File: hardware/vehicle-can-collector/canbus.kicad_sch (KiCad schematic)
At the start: 26 parts, among them Q701 2N7002, U701 MCP2557FD-xMF, U702 TH8056KDC-AAA-008-RE, U703 MCP2515-xSO, U704 MCP2557FD-xMF, U705 TCA9534

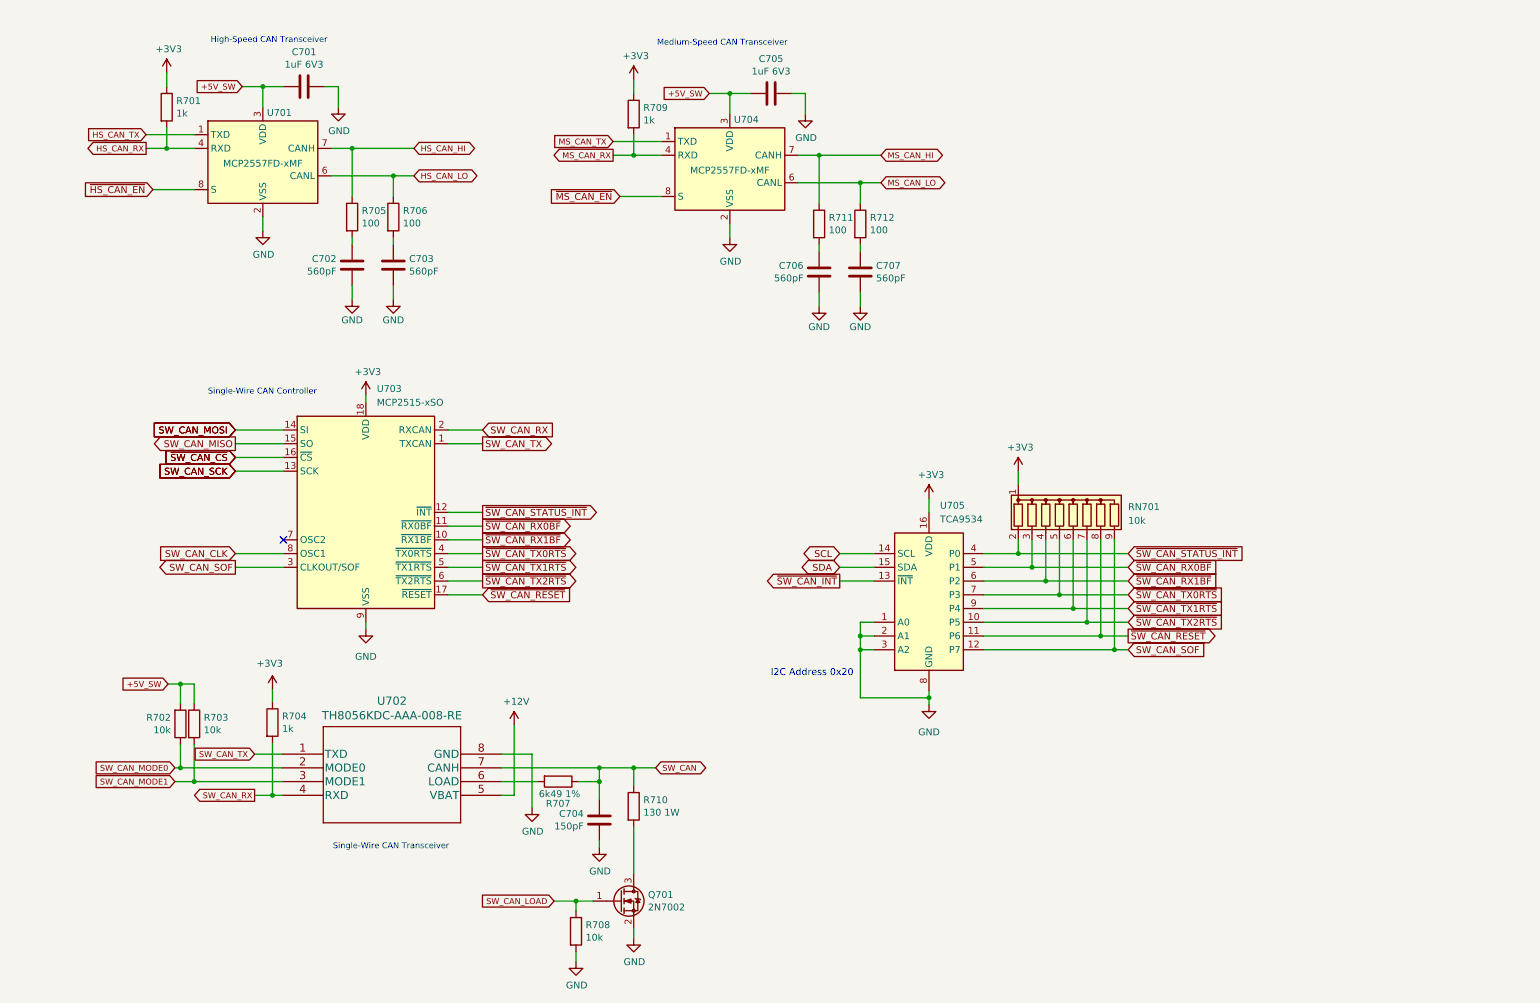
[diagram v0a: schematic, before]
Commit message: Added decoupling, more LEDs, update dts
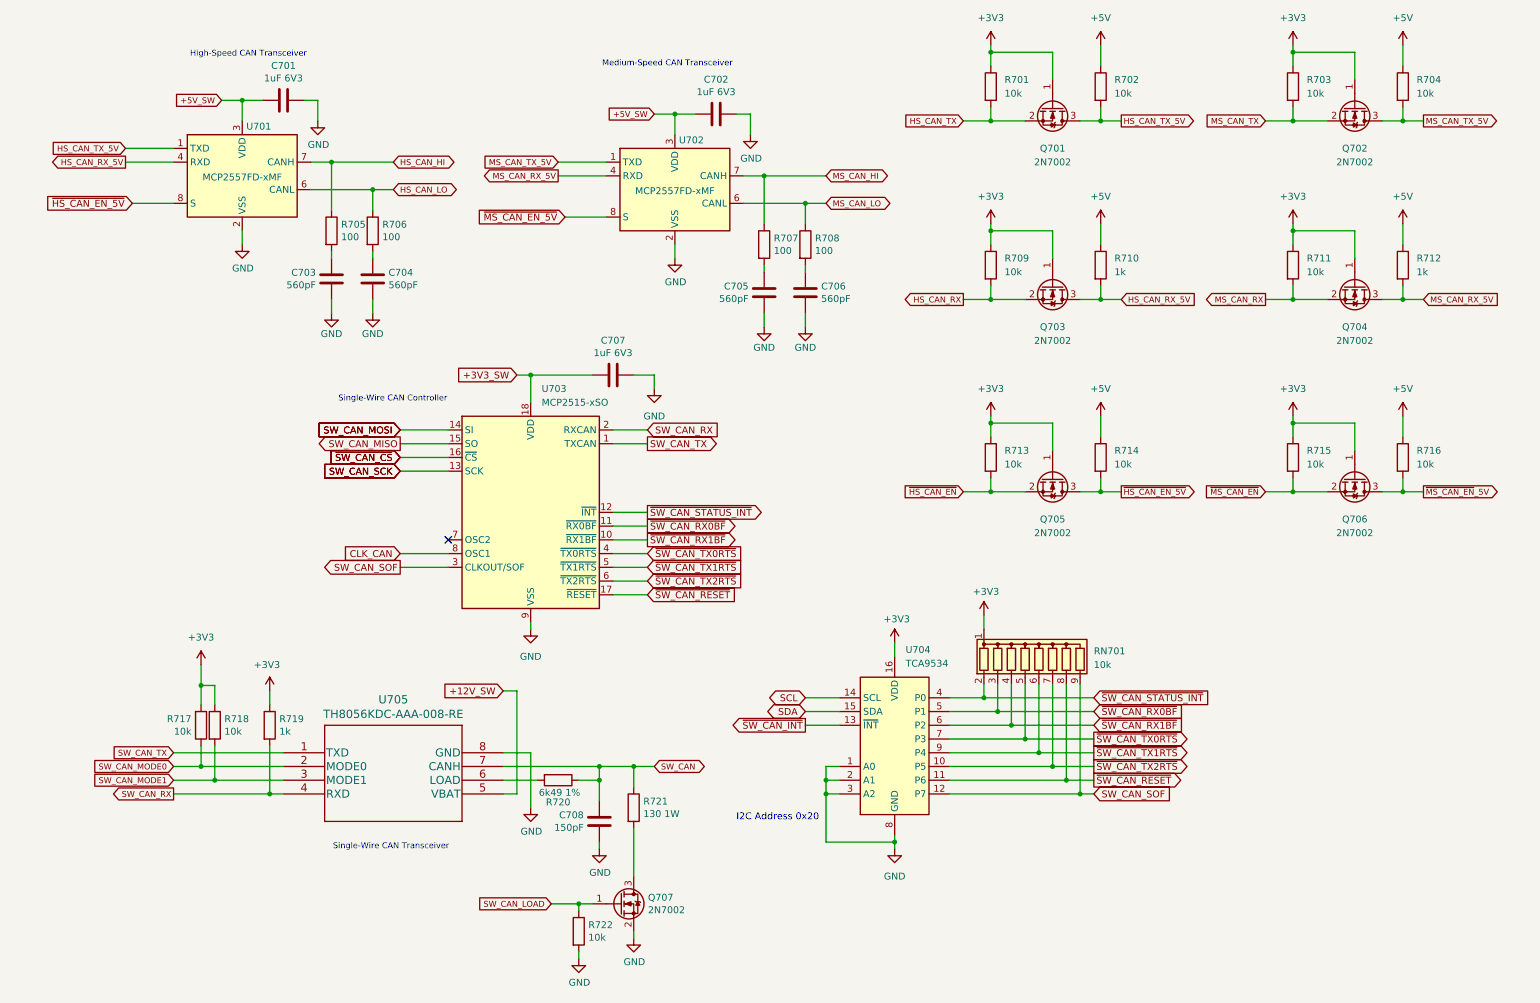
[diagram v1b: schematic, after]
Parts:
- added C707: 1uF 6V3, symbol Device:C
- added Q701, Q702, Q703, Q704, Q705, Q706: 2N7002, Package_TO_SOT_SMD:SOT-23, symbol Transistor_FET:2N7002
- added R702, R703, R704, R711, R713, R714, R715, R716: 10k, symbol Device:R
- added R710, R712: 1k, symbol Device:R
- R701, R709: value 1k -> 10k
- renumbered C705 to C702, C702 to C703, C703 to C704, C706 to C705, C707 to C706, C704 to C708, Q701 to Q707, R711 to R707, R712 to R708, R702 to R717, R703 to R718, R704 to R719, R707 to R720, R710 to R721, R708 to R722, U704 to U702, U705 to U704, U702 to U705
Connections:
- net +3V3: now also R717.2, R718.1, Q701.1 (G), Q702.1 (G), Q703.1 (G), Q704.1 (G), Q705.1 (G), Q706.1 (G), R703.1, R711.1, R713.1, R715.1; no longer U703.18 (VDD)
- net +5V_SW: no longer R717.2, R718.1
- net GND: now also C707.1
- net HS_CAN_RX: now also R709.2, Q703.2 (S); no longer R701.2, U701.4 (RXD)
- net HS_CAN_TX: now also R701.2, Q701.2 (S); no longer U701.1 (TXD)
- net MS_CAN_RX: now also Q704.2 (S), R711.2; no longer R709.2, U702.4 (RXD)
- net MS_CAN_TX: now also Q702.2 (S), R703.2; no longer U702.1 (TXD)
- net ~{HS_CAN_EN}: now also Q705.2 (S), R713.2; no longer U701.8 (S)
- net ~{MS_CAN_EN}: now also Q706.2 (S), R715.2; no longer U702.8 (S)
- net +12V renamed +12V_SW
- net SW_CAN_CLK renamed CLK_CAN
- new net +3V3_SW: C707.2, U703.18 (VDD)
- new net +5V: R702.1, R704.1, R710.1, R712.1, R714.1, R716.1
- new net HS_CAN_RX_5V: Q703.3 (D), R710.2, U701.4 (RXD)
- new net HS_CAN_TX_5V: Q701.3 (D), R702.2, U701.1 (TXD)
- new net MS_CAN_RX_5V: Q704.3 (D), R712.2, U702.4 (RXD)
- new net MS_CAN_TX_5V: Q702.3 (D), R704.2, U702.1 (TXD)
- new net ~{HS_CAN_EN_5V}: Q705.3 (D), R714.2, U701.8 (S)
- new net ~{MS_CAN_EN_5V}: U702.8 (S)
- new net ~{MS_CAN_EN}_5V: Q706.3 (D), R716.2
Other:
- company: (none) -> Gavin Hurlbut
- title: (none) -> Vehicle CAN Collector
- moved on the sheet: C701, C702, C703, C704, C705, C706, Q707, R705, R706, R707, R708, R717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

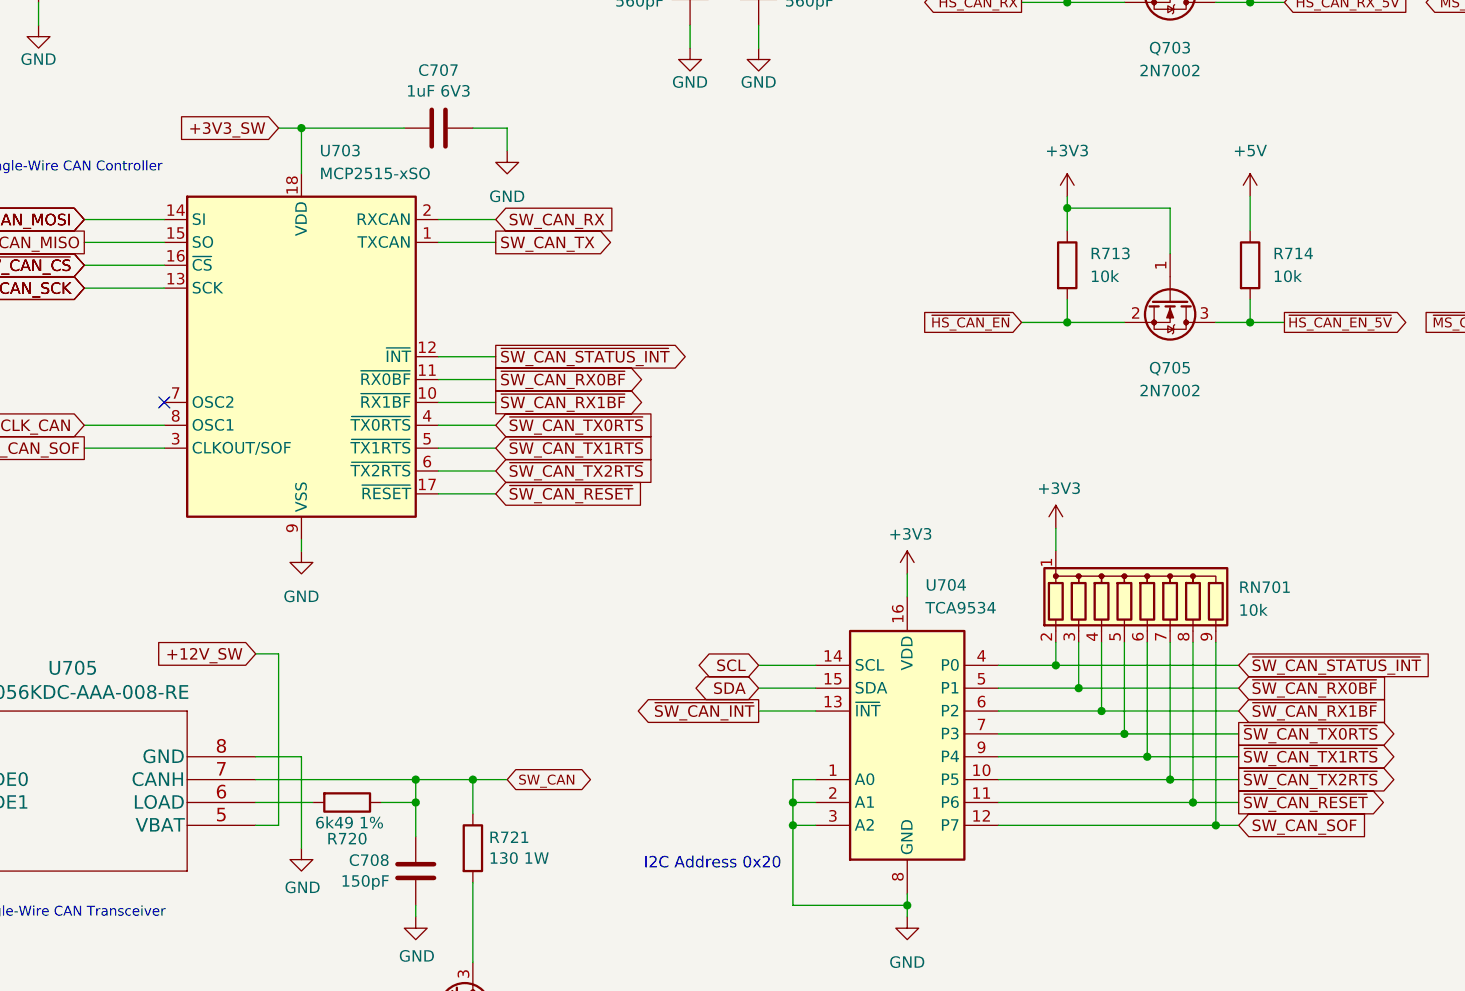
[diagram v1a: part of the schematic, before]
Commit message: Added footprints, tossed all footprints onto PCB
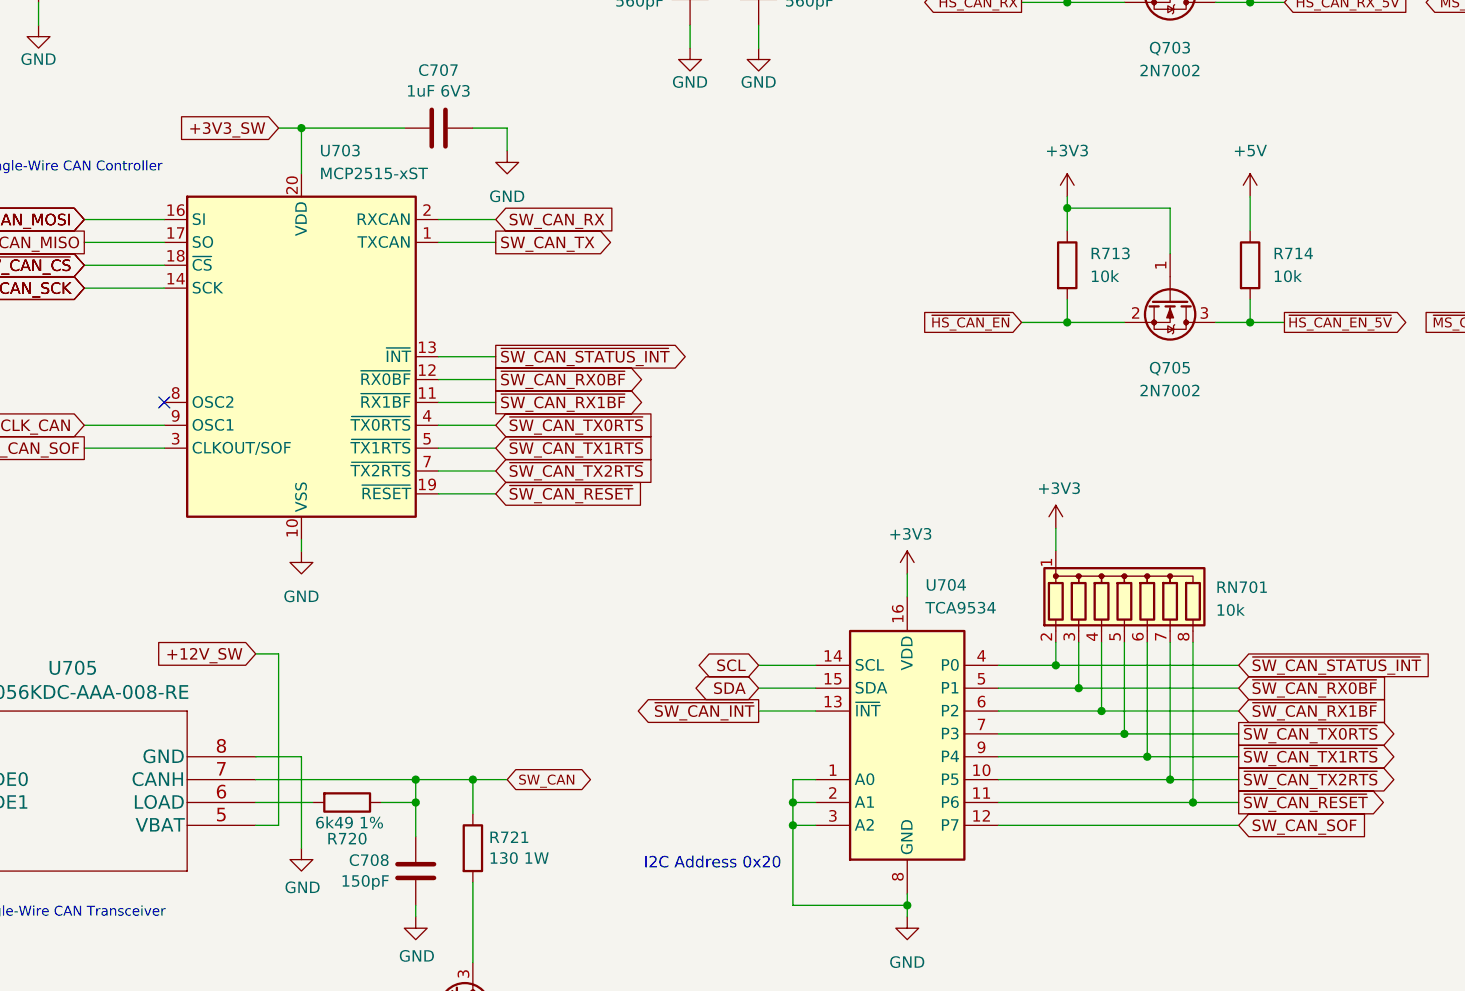
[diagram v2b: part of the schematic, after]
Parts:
- removed RN701: 10k, Resistor_THT:R_Array_SIP9, symbol Device:R_Network08
- removed U703: MCP2515-xSO, Package_SO:SOIC-18W_7.5x11.6mm_P1.27mm, symbol Interface_CAN_LIN:MCP2515-xSO
- added RN701: 10k, Resistor_THT:R_Array_SIP8, symbol Device:R_Network07
- added U703: MCP2515-xST, Package_SO:TSSOP-20_4.4x6.5mm_P0.65mm, symbol Interface_CAN_LIN:MCP2515-xST
- C701, C702, C703, C704, C705, C706, C707, C708: footprint (none) -> Capacitor_SMD:C_0805_2012Metric_Pad1.18x1.45mm_HandSolder
- R701, R702, R703, R704, R705, R706, R707, R708, R709, R710, R711, R712, R713, R714, R715, R716, R717, R718, R719, R720, R722: footprint (none) -> Resistor_SMD:R_0805_2012Metric_Pad1.20x1.40mm_HandSolder
- R721: footprint (none) -> Resistor_SMD:R_2512_6332Metric_Pad1.40x3.35mm_HandSolder
- U705: footprint MEL_SOIC-8_MEL -> UltraLibrarian:TH8056KDC-AAA-008-RE
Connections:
- net +3V3: now also RN701.1 (common)
- net +3V3_SW: now also U703.20 (VDD)
- net CLK_CAN: now also U703.9 (OSC1)
- net GND: now also U703.10 (VSS)
- net SW_CAN_CS: now also U703.18 (~{CS})
- net SW_CAN_MISO: now also U703.17 (SO)
- net SW_CAN_MOSI: now also U703.16 (SI)
- net SW_CAN_RX: now also U703.2 (RXCAN)
- net SW_CAN_SCK: now also U703.14 (SCK)
- net SW_CAN_SOF: now also U703.3 (CLKOUT/SOF)
- net SW_CAN_TX: now also U703.1 (TXCAN)
- net ~{SW_CAN_RESET}: now also RN701.8 (R7), U703.19 (~{RESET})
- net ~{SW_CAN_RX0BF}: now also RN701.3 (R2), U703.12 (~{RX0BF})
- net ~{SW_CAN_RX1BF}: now also RN701.4 (R3), U703.11 (~{RX1BF})
- net ~{SW_CAN_STATUS_INT}: now also RN701.2 (R1), U703.13 (~{INT})
- net ~{SW_CAN_TX0RTS}: now also RN701.5 (R4), U703.4 (~{TX0RTS})
- net ~{SW_CAN_TX1RTS}: now also RN701.6 (R5), U703.5 (~{TX1RTS})
- net ~{SW_CAN_TX2RTS}: now also RN701.7 (R6), U703.7 (~{TX2RTS})

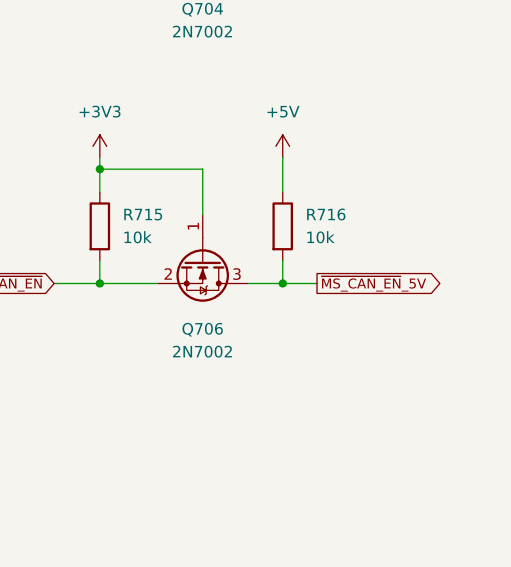
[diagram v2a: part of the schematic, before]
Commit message: Actually hook up CAN busses
- this required another pin shift.  DTS update to follow
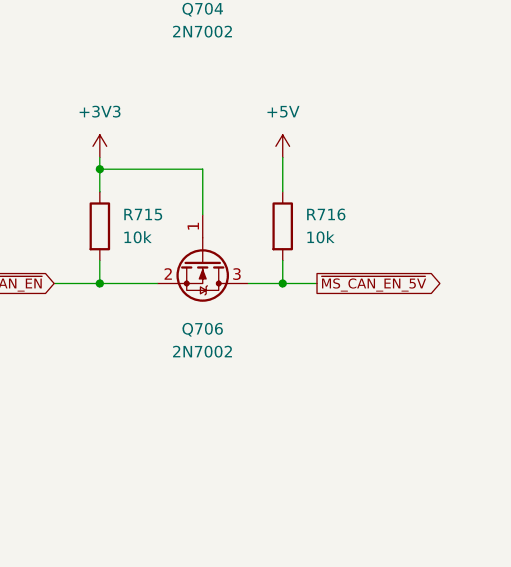
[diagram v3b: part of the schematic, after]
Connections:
- net ~{MS_CAN_EN}_5V is gone; now on net ~{MS_CAN_EN_5V}: Q706.3 (D), R716.2
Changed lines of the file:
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@@
     )
   )
-  (global_label "~{MS_CAN_EN}_5V" (shape output) (at 269.24 104.14 0) (fields_autoplaced)
+  (global_label "~{MS_CAN_EN_5V}" (shape output) (at 269.24 104.14 0) (fields_autoplaced)
     (effects (font (size 1.0922 1.0922)) (justify left))
     (property "Intersheet References" "${INTERSHEET_REFS}" (id 0) (at 283.3049 104.0718 0)
